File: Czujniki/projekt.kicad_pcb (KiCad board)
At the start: 2 copper layers, 55.9 x 45.7 mm, 57 parts, among them P1 CONN_01X08, P2 CONN_01X06, P3 CONN_01X05, U1 MCP1700, U10 PCA9306, U12 SHTC1, U14 LM4041, U15 MCP6231, U2 PIC16F1703, U3 MCP16251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

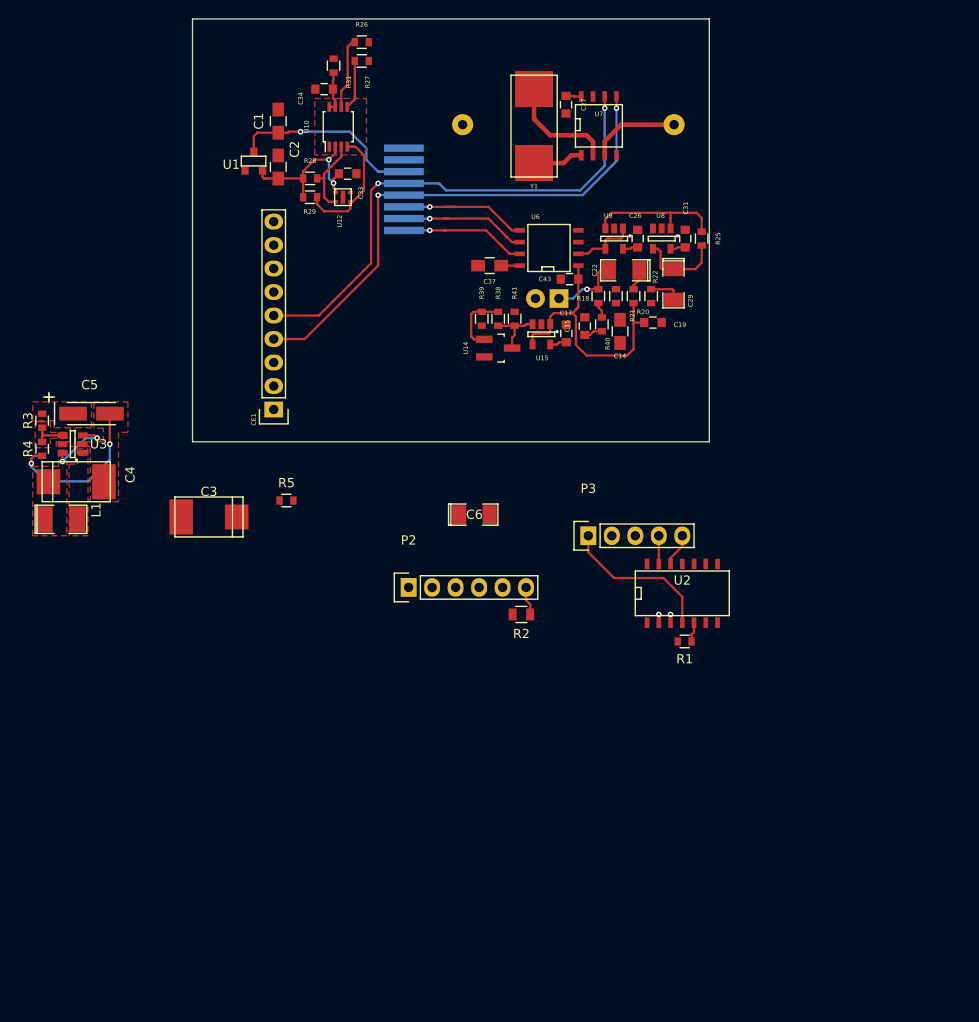
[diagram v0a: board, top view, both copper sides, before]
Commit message: Fixes after bad commit. Making bigger board.
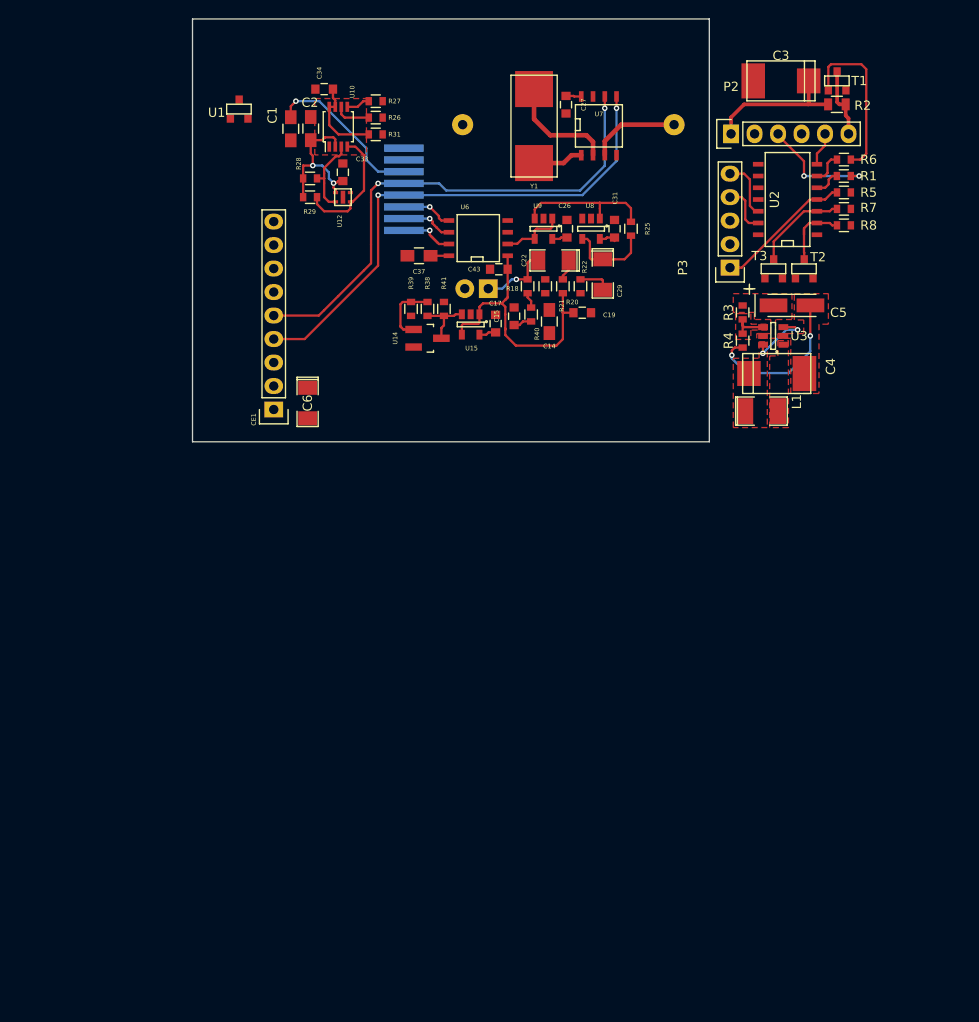
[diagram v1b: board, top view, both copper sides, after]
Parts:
- added R6: 10K, Resistors_SMD:R_0603, F.Cu at (227.9, 70.4)
- added R7: 4,7K, Resistors_SMD:R_0603, F.Cu at (227.9, 75.8)
- added R8: 4,7K, Resistors_SMD:R_0603, F.Cu at (227.9, 77.6)
- added T1: Si2323DS, Footprinty:SOT23, F.Cu at (227.2, 61.9)
- added T2: FDV303N, Footprinty:SOT23, F.Cu at (223.6, 82.3)
- added T3: FDV303N, Footprinty:SOT23, F.Cu at (220.3, 82.3)
- moved C3 77.8 mm to (221.1, 61.9)
- moved C5 76.6 mm to (222.3, 86.2)
- moved R3 76.6 mm to (217.0, 87.0)
- moved R4 76.6 mm to (217.0, 90.0)
- moved C4 76.6 mm to (220.6, 93.6)
- moved L1 76.6 mm to (219.0, 97.6)
- moved U3 76.6 mm to (220.3, 89.5)
- moved R5 68.9 mm to (227.9, 74.0)
- moved R2 64.9 mm to (227.2, 64.5)
- moved P2 60.2 mm to (215.7, 67.7)
- moved R1 53.2 mm to (227.9, 72.2), turned to 0 degrees
- moved U2 43.9 mm to (221.7, 74.8), turned to 90 degrees
- moved P3 32.8 mm to (215.6, 82.1), turned to 90 degrees
- moved C6 21.7 mm to (169.9, 96.8), turned to 270 degrees
- moved R31 8.72 mm to (177.3, 67.7), turned to 180 degrees
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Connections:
- P2 pad 6: +5V -> Net-(P2-Pad6)
- R2 pad 1: +5V -> Net-(P2-Pad6)
- U2 pad 2: SCL -> SCL5
- U2 pad 3: SDA -> SDA5
- U2 pad 6: (no net) -> CONTROL
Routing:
- net Net-(R6-Pad2): track 0.00 -> 18.0 mm
- net Net-(C3-Pad1): track 0.00 -> 15.4 mm
- net Net-(P2-Pad3): track 0.00 -> 12.6 mm, vias 0 -> 2
- net SDA5: track 0.00 -> 11.1 mm
- net SUSPEND: track 14.6 -> 5.61 mm
- net ADCDATA: track 14.4 -> 5.61 mm
- net SCL5: track 0.00 -> 7.84 mm
- net Net-(P2-Pad6): track 0.00 -> 7.74 mm
- net CLOCK: track 14.0 -> 6.77 mm
- net Net-(C34-Pad1): track 4.48 -> 9.34 mm
- net SCL: track 63.9 -> 59.2 mm, vias 3 -> 2
- net DUSTOUT: track 0.00 -> 3.65 mm
- net SDA: track 62.7 -> 59.1 mm, vias 3 -> 2
- net CONTROL: track 0.00 -> 3.54 mm
- net +5V: track 3.10 -> 0.00 mm
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
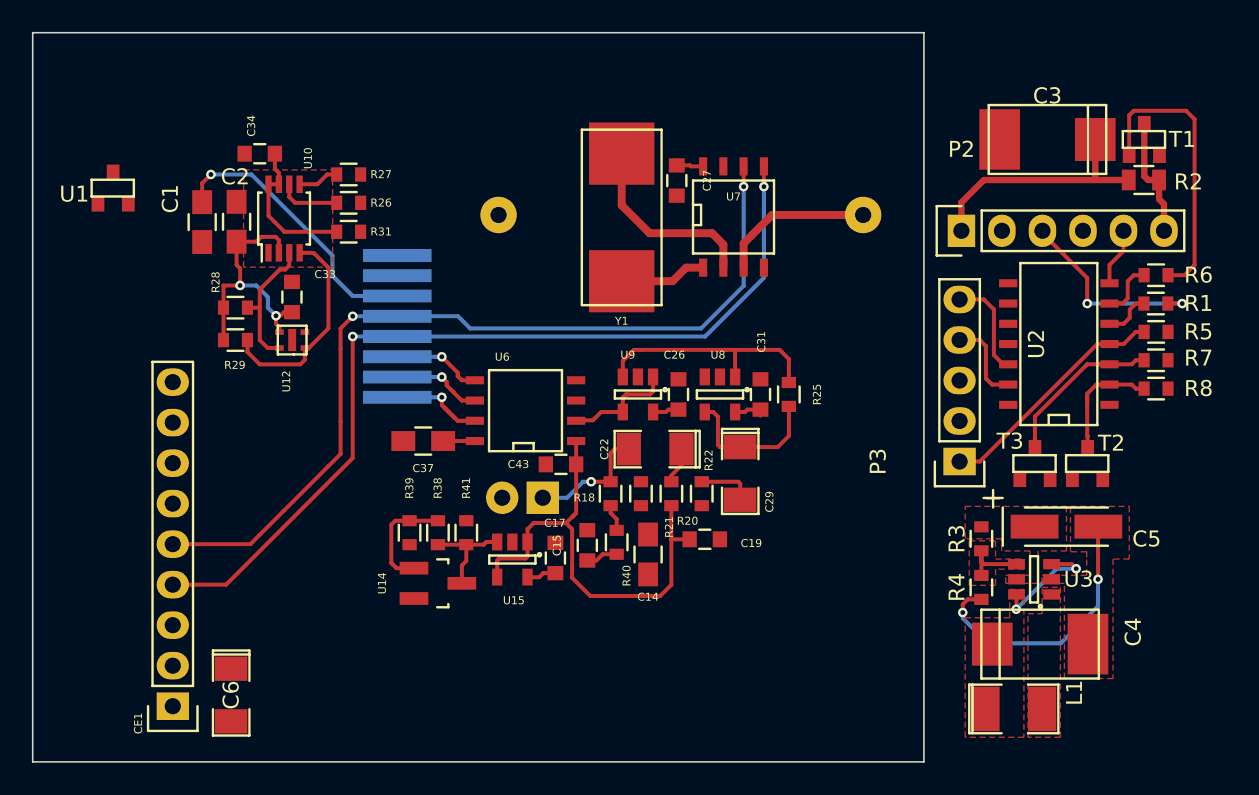
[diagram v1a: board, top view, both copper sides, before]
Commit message: Supply on sensor board done. Before gas sensor adding.
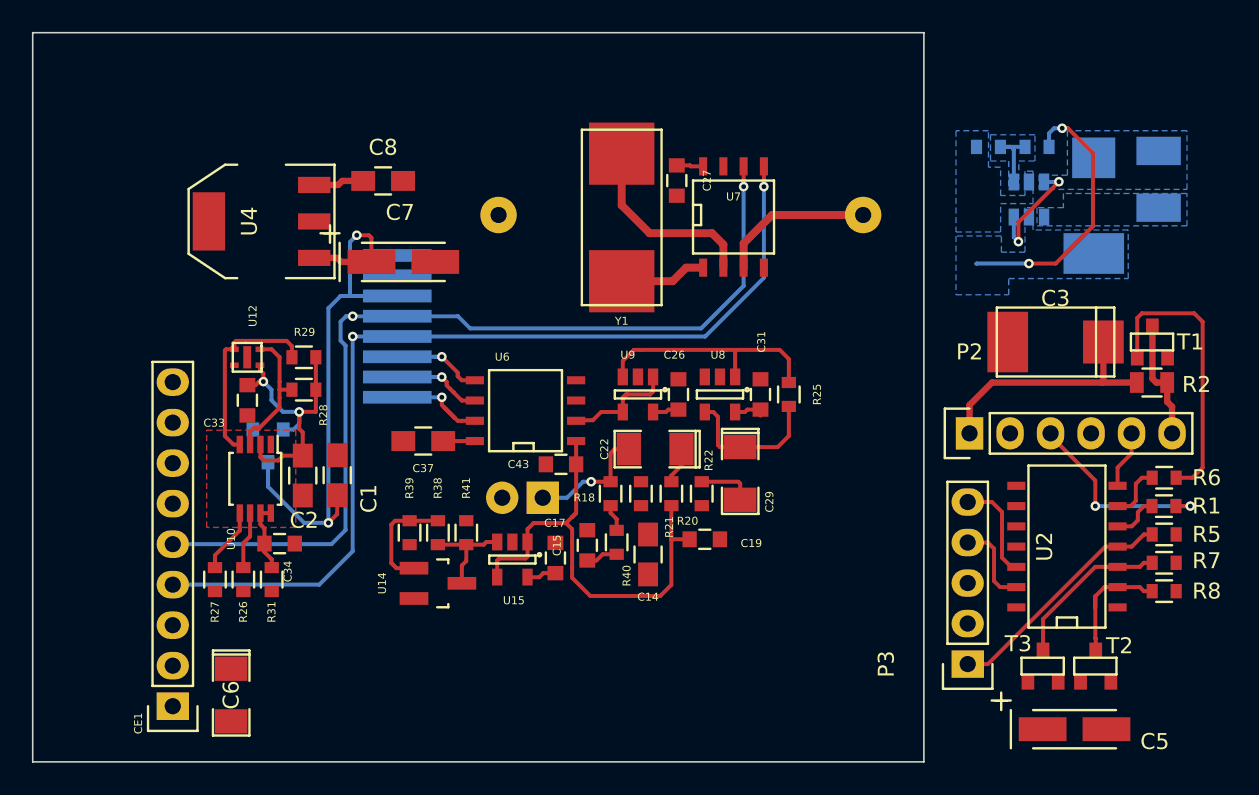
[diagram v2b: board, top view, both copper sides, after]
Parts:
- added C7: 4,7U, Capacitors_Tantalum_SMD:TantalC_SizeA_EIA-3216_HandSoldering, F.Cu at (180.7, 69.6)
- added C8: 1U, Capacitors_SMD:C_0805_HandSoldering, F.Cu at (179.5, 64.5)
- added U4: MCP1825, SMD_Packages:SOT-223, F.Cu at (171.8, 67.1)
- C4, L1, R3, R4, U1, U3: moved to B.Cu
- moved L1 34.4 mm to (228.1, 64.4), turned to 270 degrees
- moved R4 27.8 mm to (220.5, 62.4), turned to 0 degrees
- moved C4 27.7 mm to (224.0, 66.1), turned to 90 degrees
- moved R27 26.7 mm to (168.9, 89.5), turned to 270 degrees
- moved R3 24.6 mm to (217.4, 62.4), turned to 0 degrees
- moved R26 24.5 mm to (170.7, 89.5), turned to 270 degrees
- moved C34 24.5 mm to (173.0, 87.3), turned to 0 degrees
- moved U3 23.8 mm to (219.9, 65.7), turned to 90 degrees
- moved R31 22.3 mm to (172.5, 89.5), turned to 90 degrees
- moved U1 18.9 mm to (172.2, 81.2)
- moved C1 18.0 mm to (176.6, 83.0), turned to 90 degrees
- moved C2 16.4 mm to (174.4, 83.0), turned to 270 degrees
- moved U10 16.4 mm to (171.4, 83.2), turned to 270 degrees
- moved C3 12.7 mm to (221.6, 74.6)
- moved P2 12.7 mm to (216.2, 80.4)
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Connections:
- C6 pad 1: VDD2 -> VDD
- CE1 pad 2: VDD2 -> VDD
- P1 pad 7: VDD2 -> VDD
- R26 pad 2: VDD2 -> VDD
- R27 pad 2: VDD2 -> VDD
- R31 pad 1: VDD2 -> VDD
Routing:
- net MAIN_VOL: track 25.0 -> 43.9 mm, vias 3 -> 4
- net Net-(C34-Pad1): track 9.34 -> 4.36 mm
- net SDA: track 59.1 -> 64.0 mm
- net VDD: track 11.2 -> 14.4 mm
- net SCL: track 59.2 -> 62.3 mm
- net +1V8: track 16.6 -> 18.5 mm
- net SDA1.8: track 13.4 -> 12.3 mm
- added copper zone on B.Cu, net +5V
- added copper zone on B.Cu, net GND
- added copper zone on B.Cu, net MAIN_VOL
- added copper zone on B.Cu, net Net-(L1-Pad2)
- added copper zone on B.Cu, net Net-(R3-Pad2)
- removed copper zone on F.Cu, net +5V
- removed copper zone on F.Cu, net MAIN_VOL
- removed copper zone on F.Cu, net Net-(L1-Pad2)
- removed copper zone on F.Cu, net Net-(R3-Pad2)

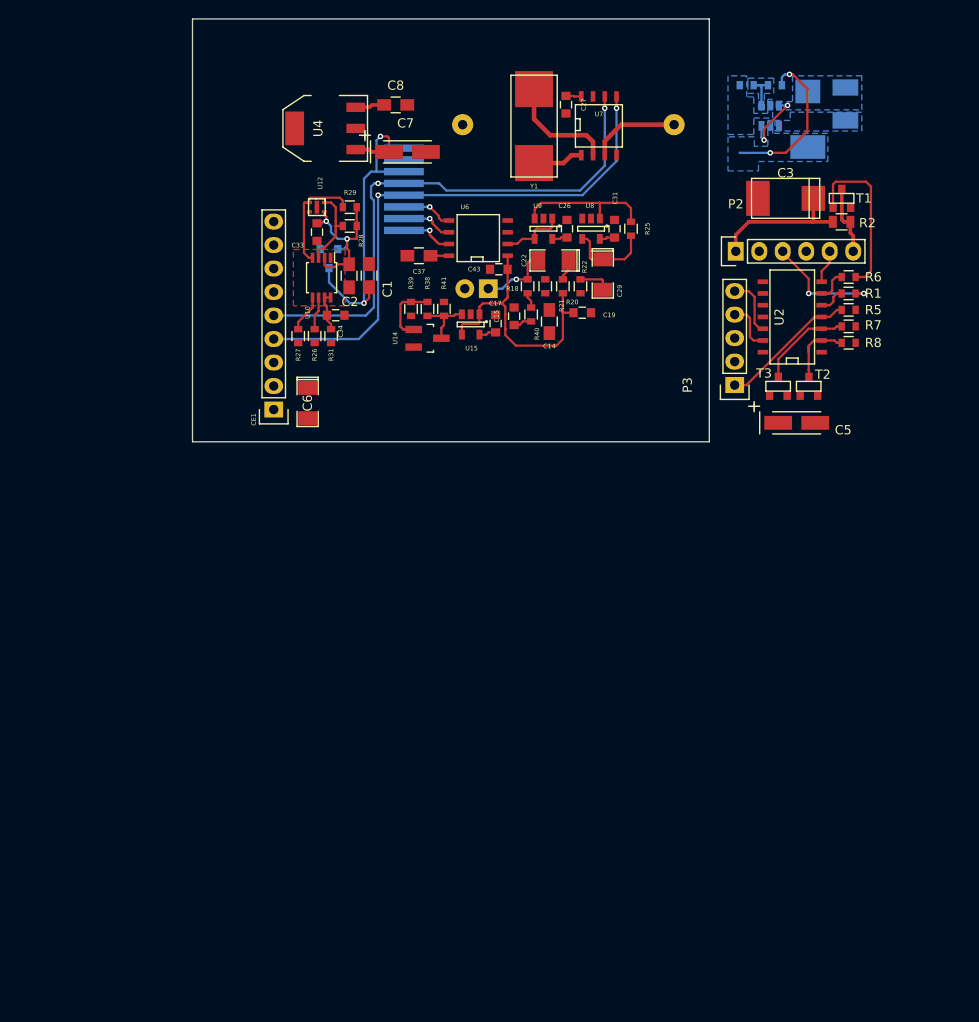
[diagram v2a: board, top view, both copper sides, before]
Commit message: Sensor added in board.
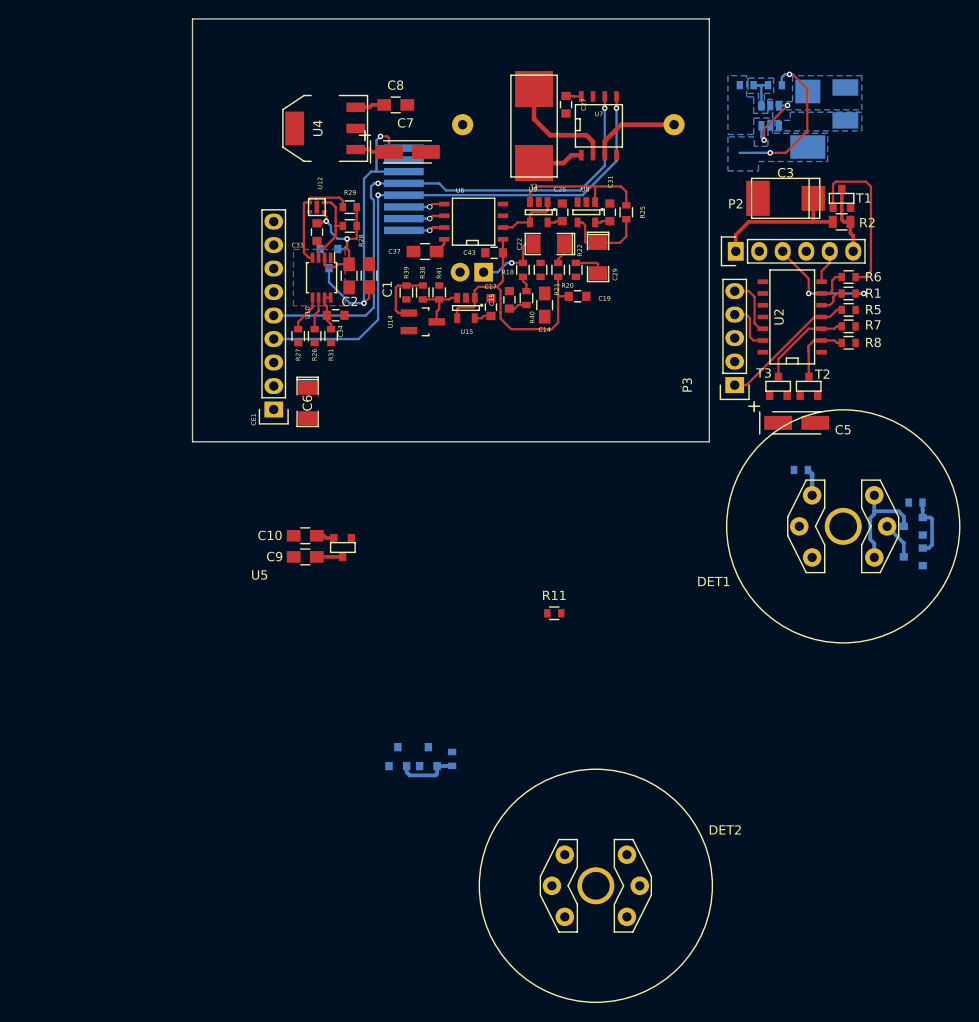
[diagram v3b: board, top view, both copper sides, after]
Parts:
- added C10: 1U, Capacitors_SMD:C_0805_HandSoldering, F.Cu at (169.7, 111.1)
- added C9: 1U, Capacitors_SMD:C_0805_HandSoldering, F.Cu at (169.7, 113.4)
- added DET1: MQ-Sensor, Footprinty:MQ-sensor, F.Cu at (227.8, 110.1)
- added DET2: MQ-Sensor, Footprinty:MQ-sensor, F.Cu at (201.1, 149.0)
- added R10: 100K, Resistors_SMD:R_0603, B.Cu at (235.7, 107.5)
- added R11: R, Resistors_SMD:R_0603, F.Cu at (196.6, 119.5)
- added R12: 100K, Resistors_SMD:R_0603, B.Cu at (185.5, 135.3)
- added R9: 4,7K, Resistors_SMD:R_0603, B.Cu at (223.3, 104.0)
- added T4: Si2323DS, Footprinty:SOT23, B.Cu at (235.4, 110.1)
- added T5: Si2323DS, Footprinty:SOT23, B.Cu at (235.4, 113.4)
- added T6: Si2323DS, Footprinty:SOT23, B.Cu at (183.0, 135.0)
- added T7: Si2323DS, Footprinty:SOT23, B.Cu at (179.7, 135.0)
- added U5: MCP1702, Footprinty:SOT23-mcp1700, F.Cu at (173.7, 112.4)
- moved C17 1.85 mm to (189.7, 86.4)
- moved C19 1.85 mm to (199.1, 85.2)
- moved C22 1.85 mm to (196.0, 79.6)
- moved C26 1.85 mm to (197.5, 76.1)
- moved C29 1.85 mm to (201.3, 81.1)
- moved C31 1.85 mm to (202.6, 76.1)
- moved C43 1.85 mm to (190.1, 80.5)
- moved R25 1.85 mm to (204.4, 76.1)
- moved R38 1.85 mm to (182.4, 84.8)
- moved R41 1.85 mm to (184.2, 84.8)
- moved U15 1.85 mm to (187.0, 86.5)
- moved U9 1.85 mm to (194.9, 76.1)
- moved C14 1.85 mm to (195.6, 86.2)
- moved C15 1.85 mm to (191.7, 85.6)
- moved R18 1.85 mm to (193.2, 82.4)
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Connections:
- U2 pad 10: (no net) -> SENSAN1
- U2 pad 11: (no net) -> SENSAN2
- U2 pad 8: (no net) -> DRV1
- U2 pad 9: (no net) -> DRV2
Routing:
- net Net-(DET1-PadA): track 0.00 -> 12.4 mm
- net Net-(R10-Pad1): track 0.00 -> 6.64 mm
- net Net-(R12-Pad1): track 0.00 -> 6.64 mm
- net Net-(DET1-PadH1): track 0.00 -> 4.04 mm
- net SENSAN1: track 0.00 -> 2.93 mm
- net VDD: track 14.4 -> 16.9 mm
- net CLOCK: track 6.77 -> 4.48 mm
- net VPP: track 0.00 -> 1.94 mm
- net ADCDATA: track 5.61 -> 4.48 mm
- net SUSPEND: track 5.61 -> 4.48 mm

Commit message: All things on PCB.
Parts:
- removed DET2: MQ-Sensor, Footprinty:MQ-sensor
- removed R11: R, Resistors_SMD:R_0603
- removed R12: 100K, Resistors_SMD:R_0603
- removed T6, T7: Si2323DS, Footprinty:SOT23
- C10, C9, U5: moved to B.Cu
- moved DET1 40.6 mm to (190.5, 94.1)
- moved R10 40.6 mm to (198.3, 91.5)
- moved R9 40.6 mm to (185.9, 88.0)
- moved T4 40.6 mm to (198.1, 94.1)
- moved T5 40.6 mm to (198.1, 97.4)
- moved C9 39.5 mm to (203.7, 93.3), turned to 90 degrees
- moved C10 36.4 mm to (201.5, 93.3), turned to 90 degrees
- moved U5 32.6 mm to (202.7, 97.4), turned to 90 degrees
- moved C5 5.97 mm to (228.1, 96.1), turned to 270 degrees
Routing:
- net SENSAN1: track 2.93 -> 50.0 mm, vias 0 -> 2
- net DRV1: track 0.00 -> 28.4 mm, vias 0 -> 1
- net Net-(R12-Pad1): track 6.64 -> 0.00 mm
- net VPP: track 1.94 -> 5.34 mm
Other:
- board size 55.9 x 45.7 mm -> 74.9 x 45.7 mm
